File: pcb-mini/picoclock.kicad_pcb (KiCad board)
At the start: 4 copper layers, 140 x 54 mm, 130 parts, among them J1 UART, J10 USB, J11 Alt Power, J12 LED_5V, J13 ESP32_IO0, J14 SJ2-35863B1-SMT-TR, J15 Conn_01x24, J2 USB_A, J3 UART, J4 xx, J5 Micro_SD_Card_Det1, J6 USB_C_Receptacle, J8 Conn_01x21_Pin, J9 AUDIO, Q1 BSS138, Q3 BSS138, SW1 SW_Push, SW2 SW_Push, SW3 SW_Push, SW4 SW_Push, SW5 SW_Push, SW6 SW_Push, SW7 SW_Push, U1 PCF8563T, U10 74LS157, U2 RP2350_80QFN, U3 MCP9808_MSOP, U4 PCM5100, U5 PAM8302A, U6 W25Q128JVS, U7 MCP45X1-104E, U8 NCP1117-3.3_SOT223, U9 ESP32-WROOM-E, Y1 Crystal, Y2 ABM8-272-T3

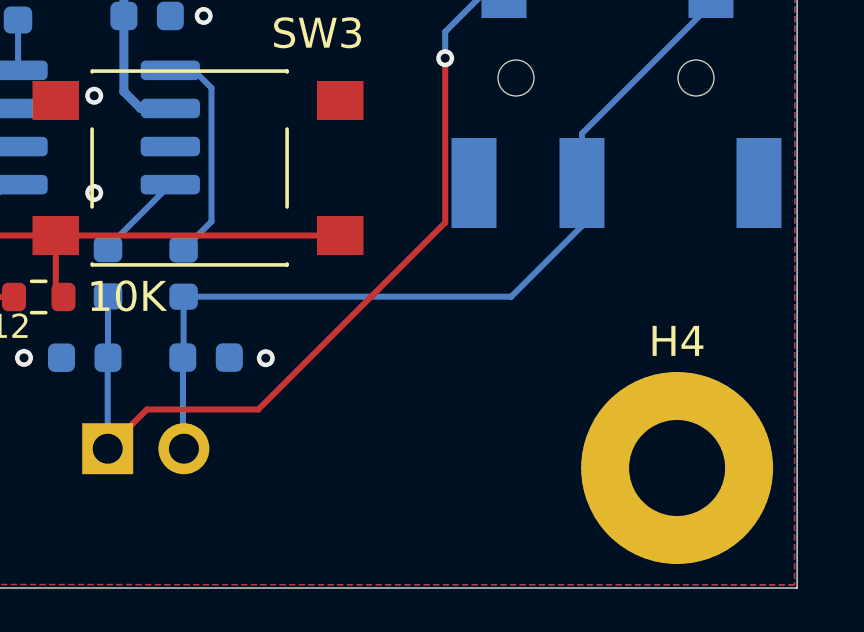
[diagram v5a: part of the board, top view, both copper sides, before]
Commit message: [pcb] mini: audio shut internal speaker when hack is connected
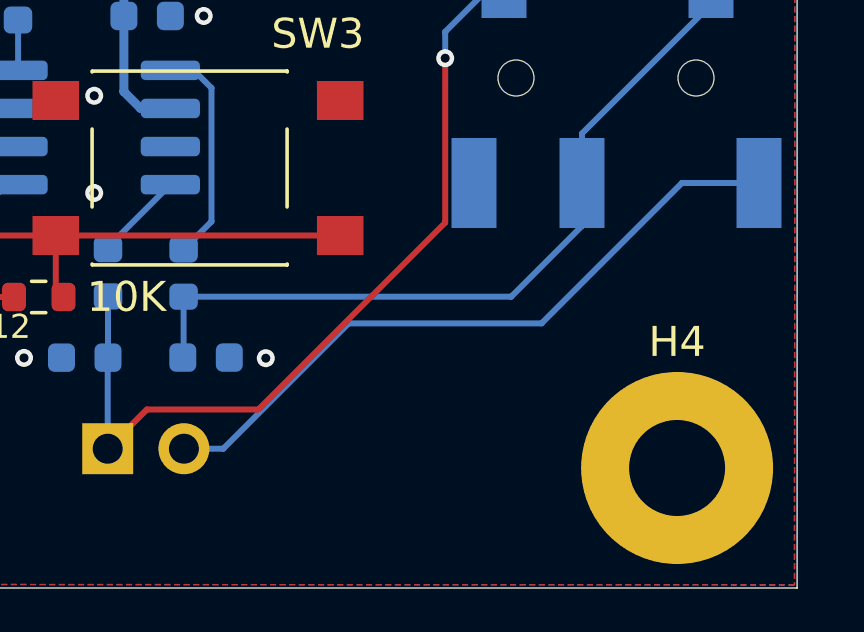
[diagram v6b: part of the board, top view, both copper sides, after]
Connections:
- J14 pad 10: unconnected-(J14-Pad10) -> SPEAKER_OUT_R+
- J9 pad 2: MONO_OUT_R+ -> SPEAKER_OUT_R+
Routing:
- net SPEAKER_OUT_R+: track 0.00 -> 22.9 mm
- net MONO_OUT_R+: track 29.6 -> 26.5 mm
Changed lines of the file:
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@@
 	(net 157 "unconnected-(J8-Pin_17-Pad17)")
 	(net 158 "unconnected-(J14-Pad4)")
-	(net 159 "unconnected-(J14-Pad10)")
+	(net 159 "SPEAKER_OUT_R+")
 	(footprint "clock:SW_SPST_TL3301TG"
 		(layer "F.Cu")
@@
 			(layers "*.Cu" "*.Mask")
 			(remove_unused_layers no)
-			(net 66 "MONO_OUT_R+")
+			(net 159 "SPEAKER_OUT_R+")
 			(pinfunction "Pin_2")
 			(pintype "passive")
@@
 			(layers "B.Cu" "B.Mask" "B.Paste")
 			(net 158 "unconnected-(J14-Pad4)")
-			(pintype "passive")
+			(pintype "passive+no_connect")
 			(solder_mask_margin 0.102)
 		)
@@
 			(size 1.5 3)
 			(layers "B.Cu" "B.Mask" "B.Paste")
-			(net 159 "unconnected-(J14-Pad10)")
+			(net 159 "SPEAKER_OUT_R+")
 			(pintype "passive")
 			(solder_mask_margin 0.102)
@@
 	)
 	(segment
-		(start 199.53 126.2875)
-		(end 199.53 129.3275)
-		(width 0.2)
-		(layer "B.Cu")
-		(net 66)
-	)
-	(segment
 		(start 199.55 124.29)
 		(end 210.47 124.29)
@@
 	)
 	(segment
-		(start 199.53 129.3275)
-		(end 199.56 129.3575)
-		(width 0.2)
-		(layer "B.Cu")
-		(net 66)
-	)
-	(segment
 		(start 158.52 125.715)
 		(end 158.565 125.76)
@@
 		(net 151)
 	)
+	(segment
+		(start 216.16 120.5)
+		(end 218.73 120.5)
+		(width 0.2)
+		(layer "B.Cu")
+		(net 159)
+	)
+	(segment
+		(start 199.56 129.3575)
+		(end 200.8725 129.3575)
+		(width 0.2)
+		(layer "B.Cu")
+		(net 159)
+	)
+	(segment
+		(start 211.48 125.18)
+		(end 216.16 120.5)
+		(width 0.2)
+		(layer "B.Cu")
+		(net 159)
+	)
+	(segment
+		(start 200.8725 129.3575)
+		(end 205.05 125.18)
+		(width 0.2)
+		(layer "B.Cu")
+		(net 159)
+	)
+	(segment
+		(start 199.53 129.3275)
+		(end 199.56 129.3575)
+		(width 0.2)
+		(layer "B.Cu")
+		(net 159)
+	)
+	(segment
+		(start 205.05 125.18)
+		(end 211.48 125.18)
+		(width 0.2)
+		(layer "B.Cu")
+		(net 159)
+	)
 	(zone

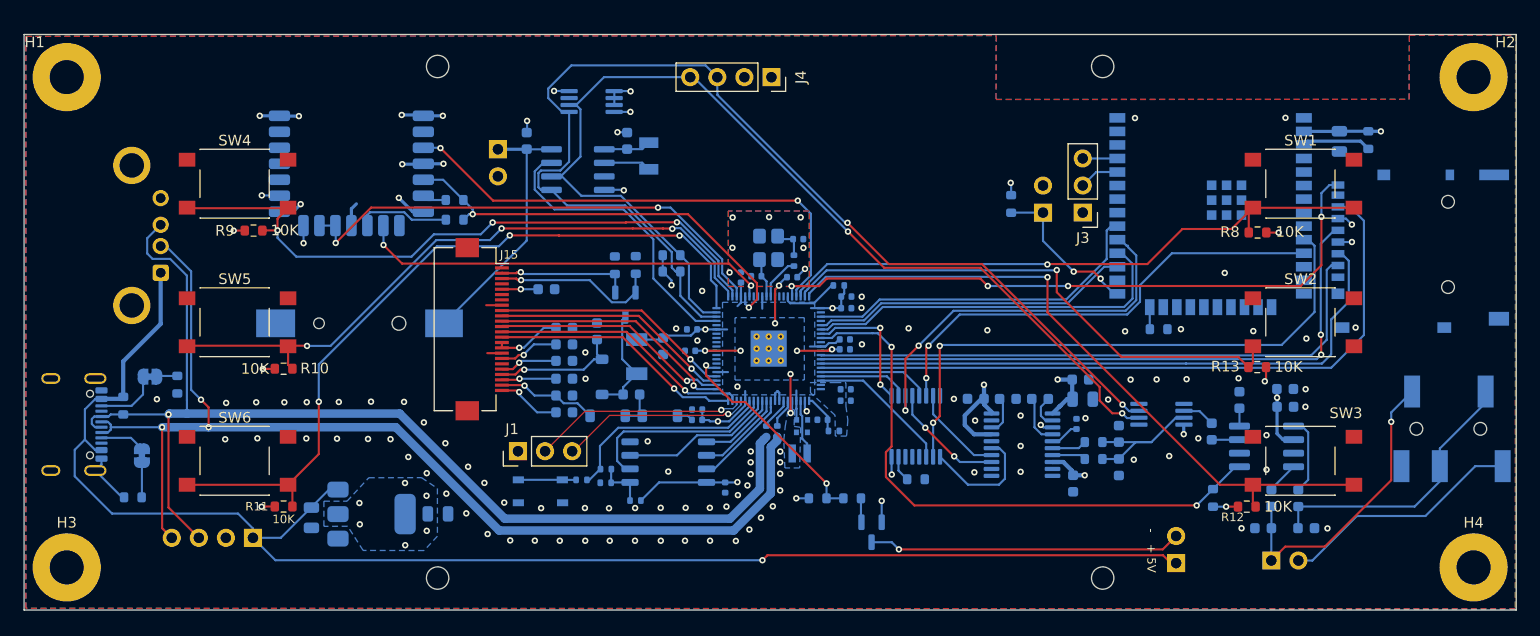
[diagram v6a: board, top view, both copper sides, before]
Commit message: [pcb] add leds
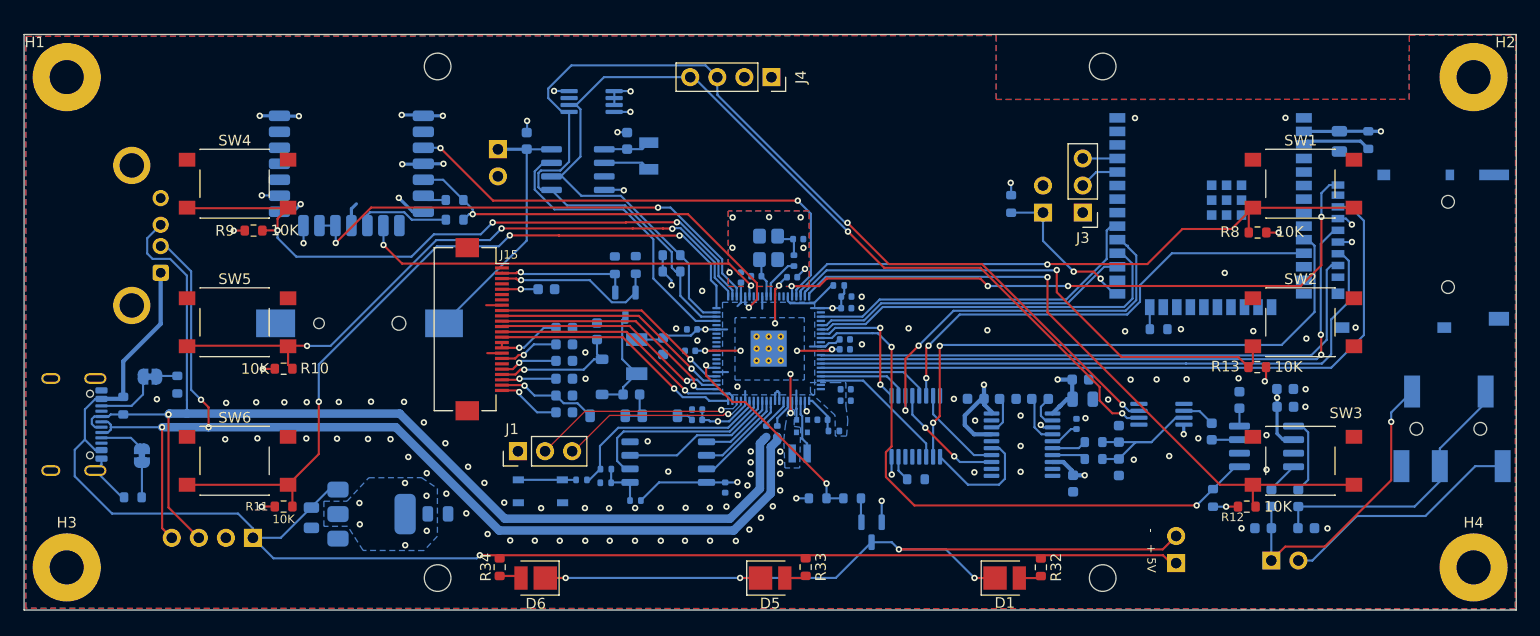
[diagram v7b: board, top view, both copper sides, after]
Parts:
- added D1: LED, LED_SMD:LED_PLCC_2835, F.Cu at (172.0, 131.0)
- added D5: LED, LED_SMD:LED_PLCC_2835, F.Cu at (150.0, 131.0)
- added D6: LED, LED_SMD:LED_PLCC_2835, F.Cu at (128.0, 131.0)
- added R32: 40, Resistor_SMD:R_0603_1608Metric, F.Cu at (175.4, 130.0)
- added R33: 40, Resistor_SMD:R_0603_1608Metric, F.Cu at (153.3, 130.0)
- added R34: 40, Resistor_SMD:R_0603_1608Metric, F.Cu at (124.6, 130.0)
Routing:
- net LED_5V-: track 29.4 -> 73.4 mm, vias 1 -> 4
- net Net-(D1-A): track 0.00 -> 2.10 mm
- net Net-(D6-A): track 0.00 -> 2.09 mm
- net Net-(D5-A): track 0.00 -> 2.04 mm
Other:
- outline, holes or cut-outs redrawn
